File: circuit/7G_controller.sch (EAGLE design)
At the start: 22 parts, among them Q1 32768Hz, T1 TPS1101D

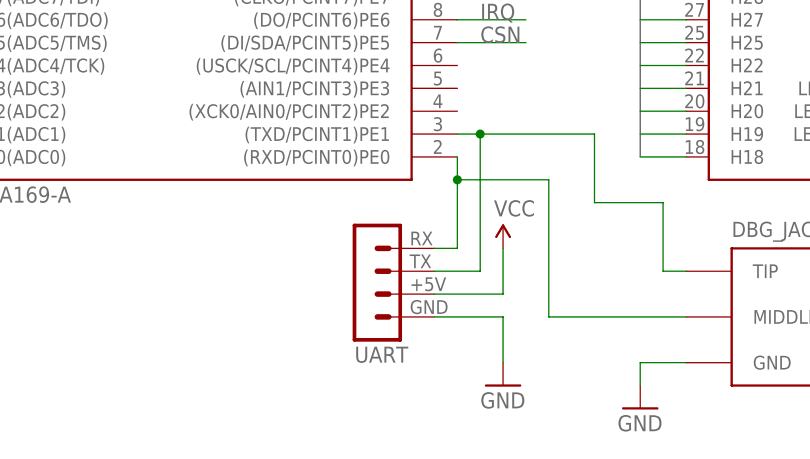
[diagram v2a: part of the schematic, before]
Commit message: 
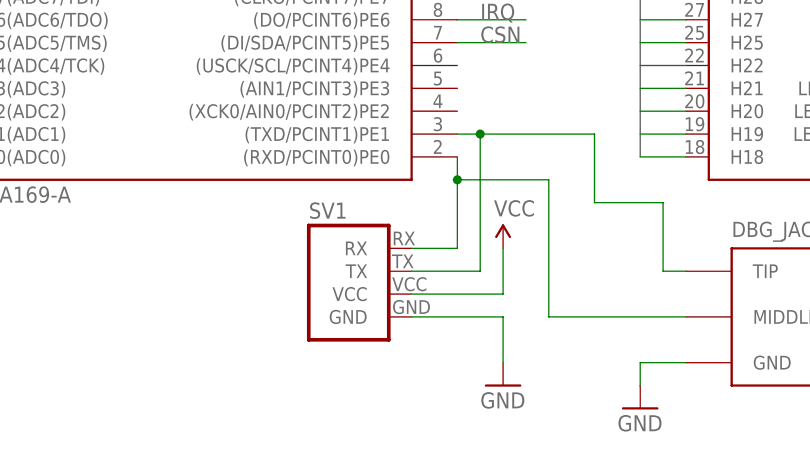
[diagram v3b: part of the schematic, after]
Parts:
- removed UART: (no value), KileParts:UART_PORT
- added SV1: (no value), KileParts:UART_PORT
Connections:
- net GND: now also SV1.GND; no longer UART.RX
- net N$29: now also SV1.RX; no longer UART.GND
- net N$30: now also SV1.TX; no longer UART.+5V
- net VCC: now also SV1.VCC; no longer UART.TX
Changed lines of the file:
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@@
 <?xml version="1.0" encoding="utf-8"?>
 <!DOCTYPE eagle SYSTEM "eagle.dtd">
-<eagle version="6.5.0">
+<eagle version="6.4">
 <drawing>
 <settings>
@@
 <part name="GND5" library="SparkFun" deviceset="GND" device=""/>
 <part name="P+7" library="SparkFun" deviceset="VCC" device=""/>
-<part name="UART" library="KileParts" deviceset="UART_PORT" device=""/>
 <part name="P+10" library="SparkFun" deviceset="VCC" device=""/>
 <part name="GND7" library="SparkFun" deviceset="GND" device=""/>
@@
 <part name="DBG_JACK" library="KileParts" deviceset="JACK_FEMALE_3.5MM" device="CHEAP"/>
 <part name="GND6" library="SparkFun" deviceset="GND" device=""/>
+<part name="SV1" library="KileParts" deviceset="UART_PORT" device=""/>
 </parts>
 <sheets>
@@
 <instance part="GND5" gate="1" x="-55.88" y="40.64"/>
 <instance part="P+7" gate="1" x="147.32" y="0"/>
-<instance part="UART" gate="1" x="43.18" y="-25.4" rot="MR180"/>
 <instance part="P+10" gate="1" x="58.42" y="-20.32"/>
 <instance part="GND7" gate="1" x="58.42" y="-35.56"/>
@@
 <instance part="DBG_JACK" gate="G$1" x="91.44" y="-30.48"/>
 <instance part="GND6" gate="1" x="73.66" y="-38.1"/>
+<instance part="SV1" gate="1" x="43.18" y="-22.86"/>
 </instances>
 <busses>
@@
 </segment>
 <segment>
-<pinref part="UART" gate="1" pin="TX"/>
-<wire x1="50.8" y1="-25.4" x2="58.42" y2="-25.4" width="0.1524" layer="91"/>
+<wire x1="48.26" y1="-25.4" x2="58.42" y2="-25.4" width="0.1524" layer="91"/>
 <wire x1="58.42" y1="-25.4" x2="58.42" y2="-20.32" width="0.1524" layer="91"/>
 <pinref part="P+10" gate="1" pin="VCC"/>
+<pinref part="SV1" gate="1" pin="VCC"/>
 </segment>
 <segment>
@@
 </segment>
 <segment>
-<pinref part="UART" gate="1" pin="RX"/>
-<wire x1="50.8" y1="-27.94" x2="58.42" y2="-27.94" width="0.1524" layer="91"/>
+<wire x1="48.26" y1="-27.94" x2="58.42" y2="-27.94" width="0.1524" layer="91"/>
 <wire x1="58.42" y1="-27.94" x2="58.42" y2="-33.02" width="0.1524" layer="91"/>
 <pinref part="GND7" gate="1" pin="GND"/>
+<pinref part="SV1" gate="1" pin="GND"/>
 </segment>
 <segment>
@@
 <pinref part="ATMEGA169PV" gate="G$1" pin="(RXD/PCINT0)PE0"/>
 <wire x1="53.34" y1="-10.16" x2="53.34" y2="-12.7" width="0.1524" layer="91"/>
-<pinref part="UART" gate="1" pin="GND"/>
 <wire x1="53.34" y1="-12.7" x2="53.34" y2="-20.32" width="0.1524" layer="91"/>
-<wire x1="50.8" y1="-20.32" x2="53.34" y2="-20.32" width="0.1524" layer="91"/>
 <pinref part="DBG_JACK" gate="G$1" pin="MIDDLE"/>
 <wire x1="78.74" y1="-27.94" x2="63.5" y2="-27.94" width="0.1524" layer="91"/>
@@
 <wire x1="63.5" y1="-12.7" x2="53.34" y2="-12.7" width="0.1524" layer="91"/>
 <junction x="53.34" y="-12.7"/>
+<pinref part="SV1" gate="1" pin="RX"/>
+<wire x1="53.34" y1="-20.32" x2="48.26" y2="-20.32" width="0.1524" layer="91"/>
 </segment>
 </net>
@@
 <wire x1="53.34" y1="-7.62" x2="55.88" y2="-7.62" width="0.1524" layer="91"/>
 <wire x1="55.88" y1="-7.62" x2="55.88" y2="-22.86" width="0.1524" layer="91"/>
-<pinref part="UART" gate="1" pin="+5V"/>
-<wire x1="55.88" y1="-22.86" x2="50.8" y2="-22.86" width="0.1524" layer="91"/>
+<wire x1="55.88" y1="-22.86" x2="48.26" y2="-22.86" width="0.1524" layer="91"/>
 <pinref part="DBG_JACK" gate="G$1" pin="TIP"/>
 <wire x1="78.74" y1="-22.86" x2="76.2" y2="-22.86" width="0.1524" layer="91"/>
@@
 <wire x1="68.58" y1="-7.62" x2="55.88" y2="-7.62" width="0.1524" layer="91"/>
 <junction x="55.88" y="-7.62"/>
-</segment>
-</net>
+<pinref part="SV1" gate="1" pin="TX"/>
+</segment>
+</net>

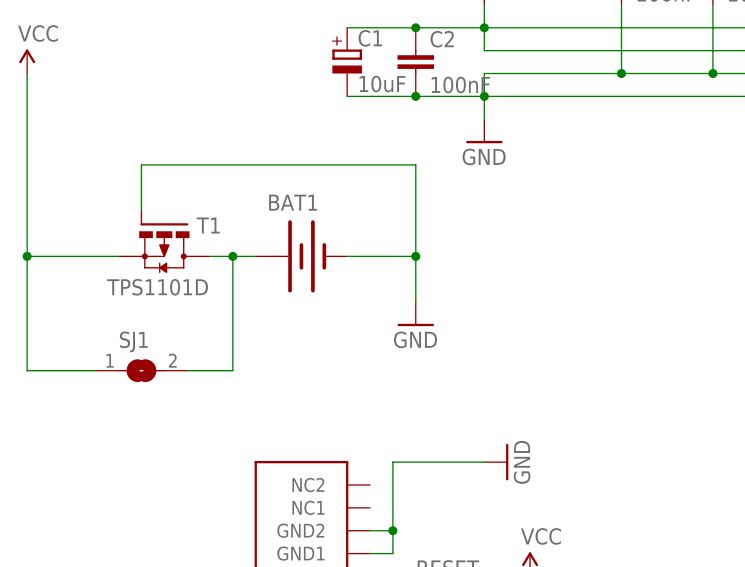
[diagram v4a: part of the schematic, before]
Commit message: CR2032 holder
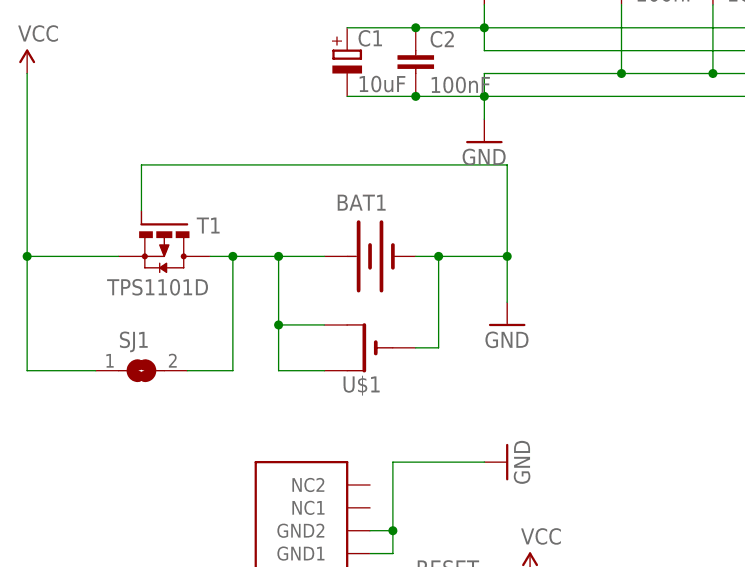
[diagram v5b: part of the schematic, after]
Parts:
- added U$1: (no value), adafruit:CR2032SMT
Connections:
- net GND: now also U$1.-
- net N$4: now also U$1.+, U$1.+1
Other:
- moved on the sheet: BAT1
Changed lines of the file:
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@@
 <part name="GND6" library="SparkFun" deviceset="GND" device=""/>
 <part name="SV1" library="KileParts" deviceset="UART_PORT" device=""/>
+<part name="U$1" library="adafruit" deviceset="CR2032" device="SMT"/>
 </parts>
 <sheets>
@@
 <instance part="P+4" gate="1" x="147.32" y="109.22"/>
 <instance part="MTRX_CONN" gate="G$1" x="91.44" y="10.16" rot="R180"/>
-<instance part="BAT1" gate="G$1" x="-68.58" y="48.26"/>
+<instance part="BAT1" gate="G$1" x="-60.96" y="48.26"/>
 <instance part="P+6" gate="1" x="-99.06" y="68.58"/>
-<instance part="GND5" gate="1" x="-55.88" y="40.64"/>
+<instance part="GND5" gate="1" x="-45.72" y="40.64"/>
 <instance part="P+7" gate="1" x="147.32" y="0"/>
 <instance part="P+10" gate="1" x="58.42" y="-20.32"/>
@@
 <instance part="GND6" gate="1" x="73.66" y="-38.1"/>
 <instance part="SV1" gate="1" x="43.18" y="-22.86"/>
+<instance part="U$1" gate="G$1" x="-60.96" y="38.1" rot="R180"/>
 </instances>
 <busses>
@@
 <segment>
 <pinref part="BAT1" gate="G$1" pin="-"/>
-<wire x1="-63.5" y1="48.26" x2="-55.88" y2="48.26" width="0.1524" layer="91"/>
-<wire x1="-55.88" y1="48.26" x2="-55.88" y2="43.18" width="0.1524" layer="91"/>
+<wire x1="-55.88" y1="48.26" x2="-53.34" y2="48.26" width="0.1524" layer="91"/>
+<wire x1="-53.34" y1="48.26" x2="-45.72" y2="48.26" width="0.1524" layer="91"/>
+<wire x1="-45.72" y1="48.26" x2="-45.72" y2="43.18" width="0.1524" layer="91"/>
 <pinref part="GND5" gate="1" pin="GND"/>
 <pinref part="T1" gate="G$1" pin="G"/>
 <wire x1="-86.36" y1="53.34" x2="-86.36" y2="58.42" width="0.1524" layer="91"/>
-<wire x1="-86.36" y1="58.42" x2="-55.88" y2="58.42" width="0.1524" layer="91"/>
-<wire x1="-55.88" y1="58.42" x2="-55.88" y2="48.26" width="0.1524" layer="91"/>
-<junction x="-55.88" y="48.26"/>
+<wire x1="-86.36" y1="58.42" x2="-45.72" y2="58.42" width="0.1524" layer="91"/>
+<wire x1="-45.72" y1="58.42" x2="-45.72" y2="48.26" width="0.1524" layer="91"/>
+<junction x="-45.72" y="48.26"/>
+<wire x1="-53.34" y1="48.26" x2="-53.34" y2="38.1" width="0.1524" layer="91"/>
+<junction x="-53.34" y="48.26"/>
+<pinref part="U$1" gate="G$1" pin="-"/>
+<wire x1="-53.34" y1="38.1" x2="-55.88" y2="38.1" width="0.1524" layer="91"/>
 </segment>
 <segment>
@@
 <pinref part="BAT1" gate="G$1" pin="+"/>
 <pinref part="T1" gate="G$1" pin="D"/>
-<wire x1="-73.66" y1="48.26" x2="-76.2" y2="48.26" width="0.1524" layer="91"/>
+<wire x1="-66.04" y1="48.26" x2="-71.12" y2="48.26" width="0.1524" layer="91"/>
 <pinref part="SJ1" gate="1" pin="2"/>
+<wire x1="-71.12" y1="48.26" x2="-76.2" y2="48.26" width="0.1524" layer="91"/>
 <wire x1="-76.2" y1="48.26" x2="-78.74" y2="48.26" width="0.1524" layer="91"/>
 <wire x1="-81.28" y1="35.56" x2="-76.2" y2="35.56" width="0.1524" layer="91"/>
 <wire x1="-76.2" y1="35.56" x2="-76.2" y2="48.26" width="0.1524" layer="91"/>
 <junction x="-76.2" y="48.26"/>
-</segment>
-</net>
+<wire x1="-71.12" y1="48.26" x2="-71.12" y2="40.64" width="0.1524" layer="91"/>
+<junction x="-71.12" y="48.26"/>
+<pinref part="U$1" gate="G$1" pin="+"/>
+<wire x1="-71.12" y1="40.64" x2="-71.12" y2="35.56" width="0.1524" layer="91"/>
+<wire x1="-71.12" y1="35.56" x2="-66.04" y2="35.56" width="0.1524" layer="91"/>
+<pinref part="U$1" gate="G$1" pin="+1"/>
+<wire x1="-66.04" y1="40.64" x2="-71.12" y2="40.64" width="0.1524" layer="91"/>
+<junction x="-71.12" y="40.64"/>
+</segment>
+</net>

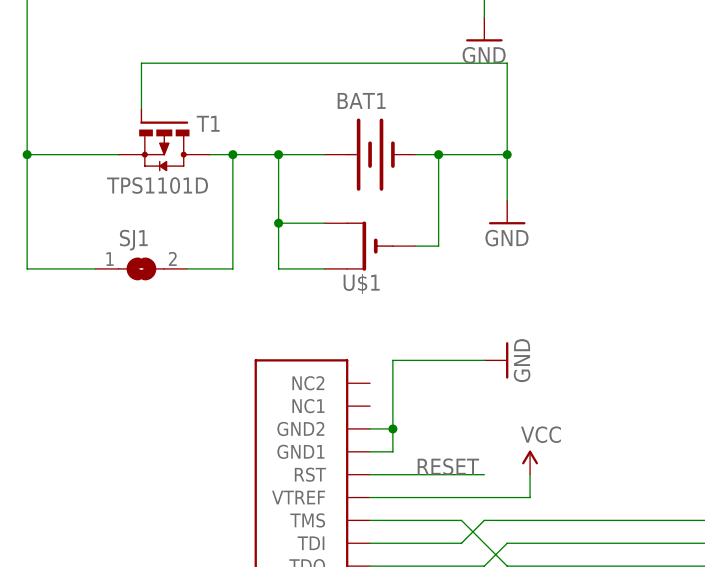
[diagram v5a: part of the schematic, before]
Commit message: finished adding the CR2032 battery holder
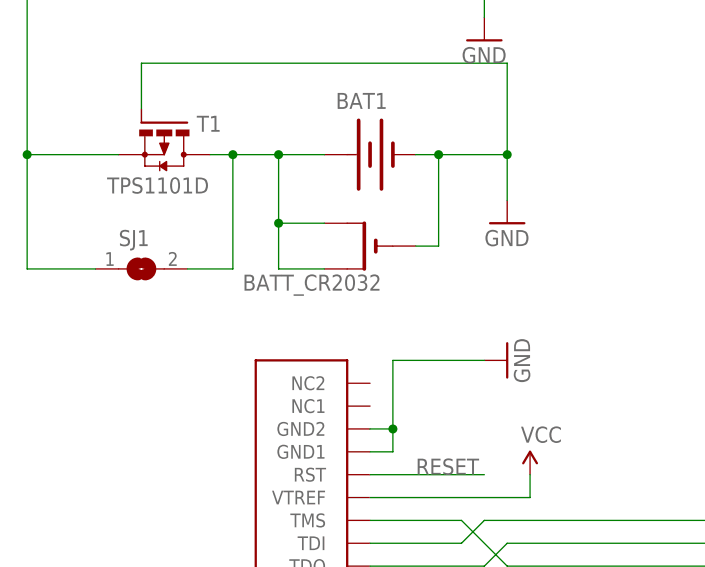
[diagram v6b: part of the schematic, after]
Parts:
- removed U$1: (no value), adafruit:CR2032SMT
- added BATT_CR2032: (no value), KileParts:CR2032SMT
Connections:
- net GND: now also BATT_CR2032.-; no longer U$1.-
- net N$4: now also BATT_CR2032.+, BATT_CR2032.+1; no longer U$1.+, U$1.+1
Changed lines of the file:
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@@
 <part name="GND6" library="SparkFun" deviceset="GND" device=""/>
 <part name="SV1" library="KileParts" deviceset="UART_PORT" device=""/>
-<part name="U$1" library="adafruit" deviceset="CR2032" device="SMT"/>
+<part name="BATT_CR2032" library="KileParts" deviceset="CR2032" device="SMT"/>
 </parts>
 <sheets>
@@
 <instance part="GND6" gate="1" x="73.66" y="-38.1"/>
 <instance part="SV1" gate="1" x="43.18" y="-22.86"/>
-<instance part="U$1" gate="G$1" x="-60.96" y="38.1" rot="R180"/>
+<instance part="BATT_CR2032" gate="G$1" x="-60.96" y="38.1" rot="R180"/>
 </instances>
 <busses>
@@
 <wire x1="-53.34" y1="48.26" x2="-53.34" y2="38.1" width="0.1524" layer="91"/>
 <junction x="-53.34" y="48.26"/>
-<pinref part="U$1" gate="G$1" pin="-"/>
+<pinref part="BATT_CR2032" gate="G$1" pin="-"/>
 <wire x1="-53.34" y1="38.1" x2="-55.88" y2="38.1" width="0.1524" layer="91"/>
 </segment>
@@
 <wire x1="-71.12" y1="48.26" x2="-71.12" y2="40.64" width="0.1524" layer="91"/>
 <junction x="-71.12" y="48.26"/>
-<pinref part="U$1" gate="G$1" pin="+"/>
+<pinref part="BATT_CR2032" gate="G$1" pin="+"/>
 <wire x1="-71.12" y1="40.64" x2="-71.12" y2="35.56" width="0.1524" layer="91"/>
 <wire x1="-71.12" y1="35.56" x2="-66.04" y2="35.56" width="0.1524" layer="91"/>
-<pinref part="U$1" gate="G$1" pin="+1"/>
+<pinref part="BATT_CR2032" gate="G$1" pin="+1"/>
 <wire x1="-66.04" y1="40.64" x2="-71.12" y2="40.64" width="0.1524" layer="91"/>
 <junction x="-71.12" y="40.64"/>
